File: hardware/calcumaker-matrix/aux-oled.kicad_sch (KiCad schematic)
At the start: 1 part, among them J3 OLED 128x32 (DNP)

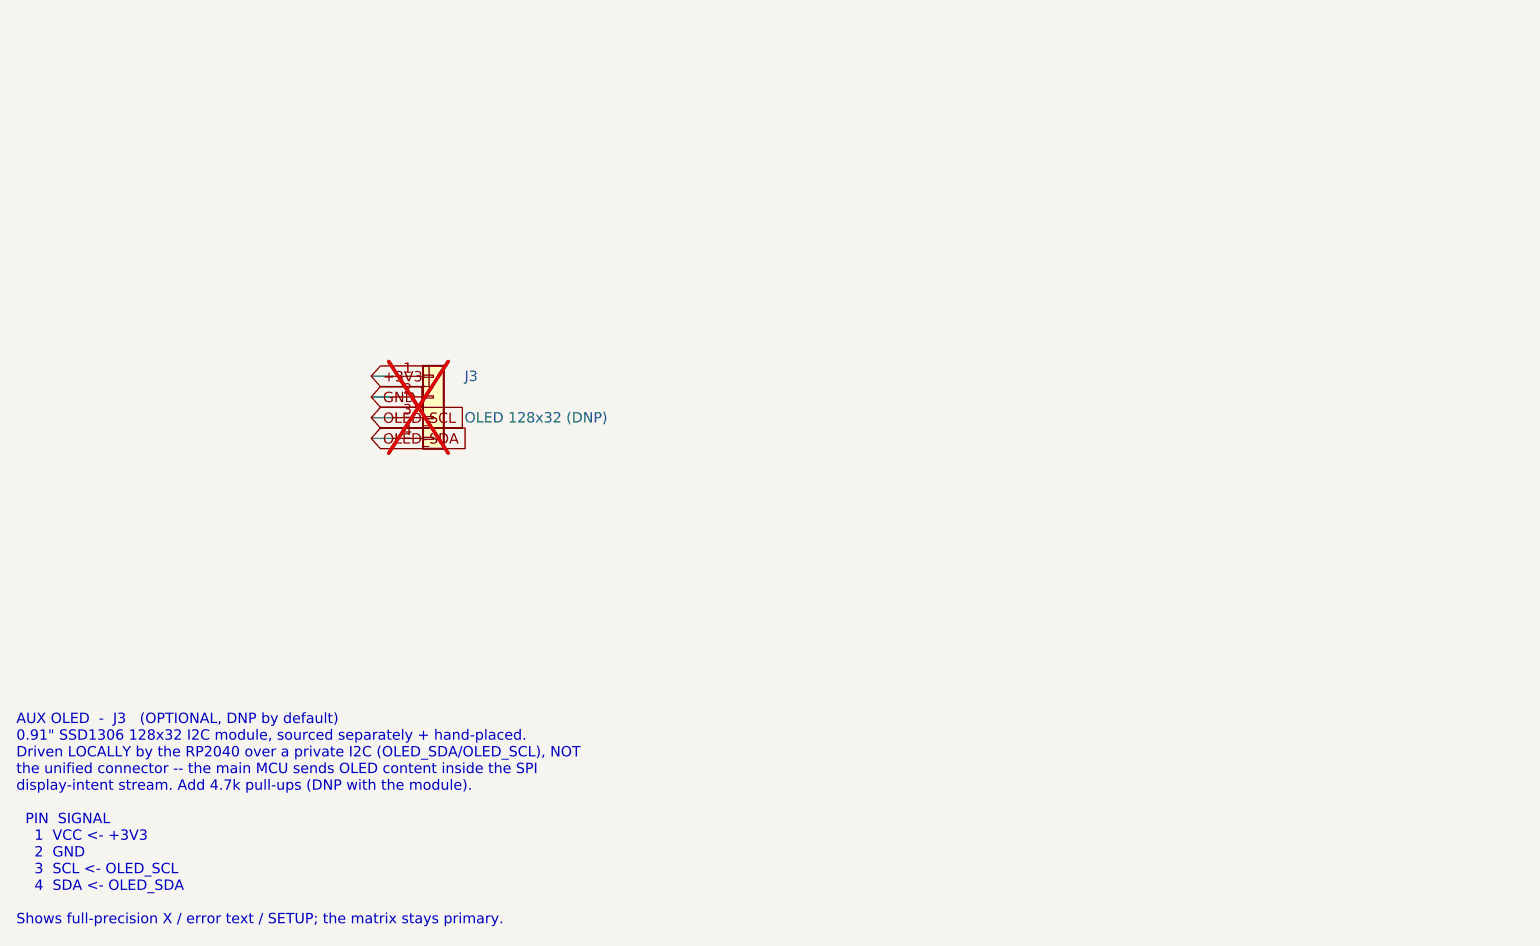
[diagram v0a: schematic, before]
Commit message: Floorplan both display PCBs and verify their schematic nets
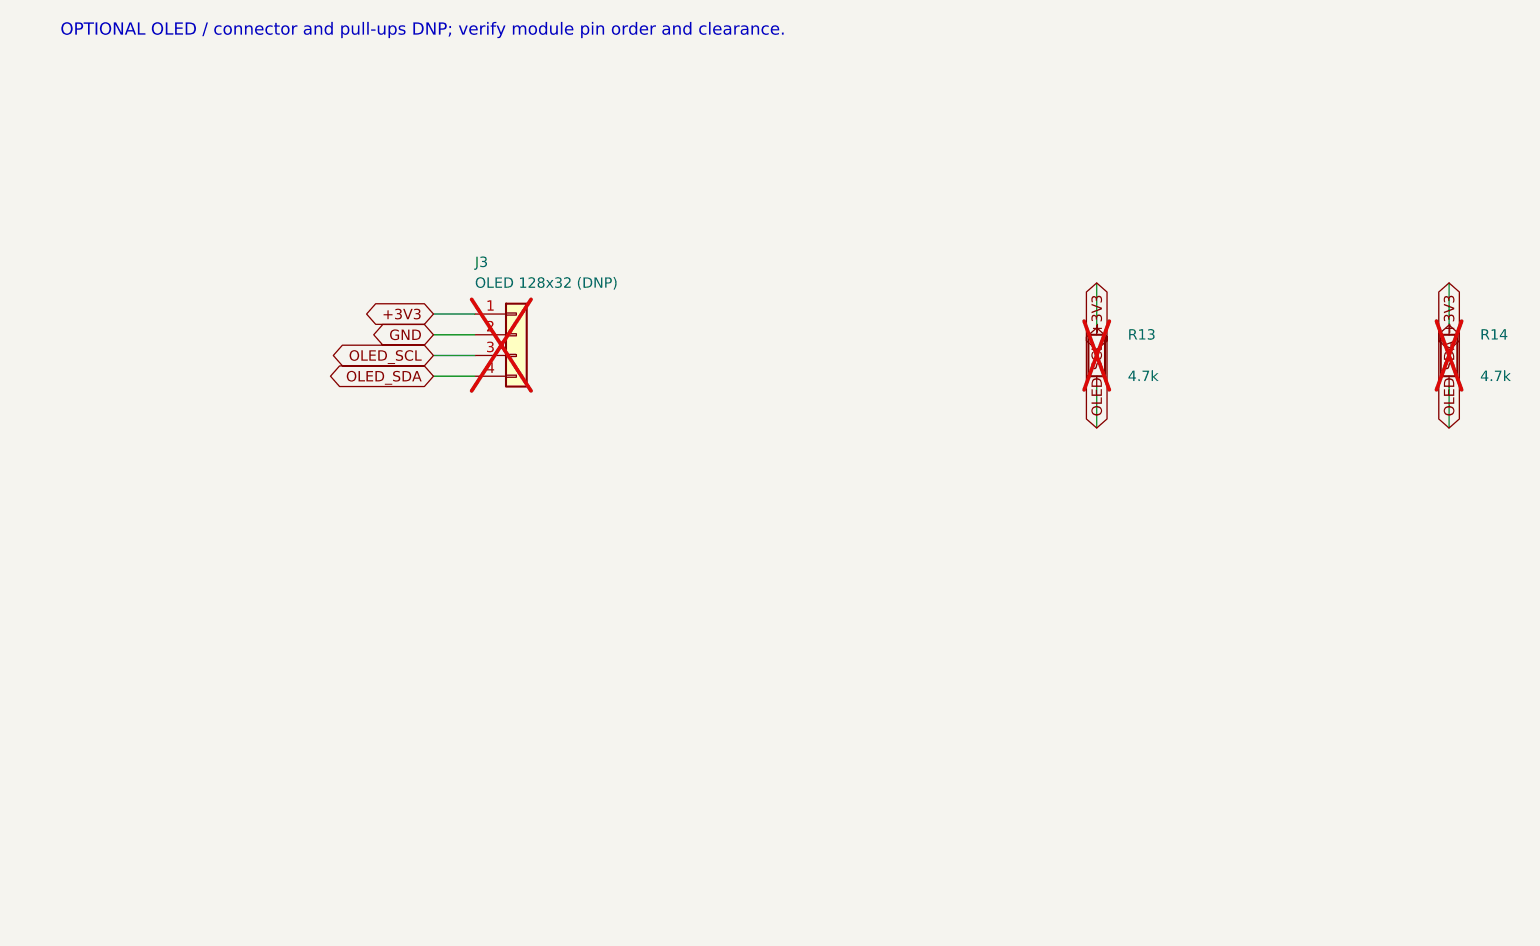
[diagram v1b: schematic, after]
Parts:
- added R13, R14: 4.7k, Resistor_SMD:R_0402_1005Metric, symbol Device:R
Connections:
- net +3V3: now also R13.1, R14.1
- net OLED_SCL: now also R13.2
- net OLED_SDA: now also R14.2
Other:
- note added: "OPTIONAL OLED / connector and pull-ups DNP; verify module pin order and clearance."
- note removed: "AUX OLED - J3 (OPTIONAL, DNP by default) 0.91" SSD1306 128x32 I2C module, sourced separately + hand-placed. Driven LOCALLY by the RP2040 over a private I2C (OLED_SDA/OLED_SCL), NOT the unified connector -- the main MCU sends OLED content inside the SPI display-intent stream. Add 4.7k pull-ups (DNP with the module). PIN SIGNAL 1 VCC <- +3V3 2 GND 3 SCL <- OLED_SCL 4 SDA <- OLED_SDA Shows full-prec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"
- title: Calcumaker 16 — RGB Matrix — Aux OLED 128x32 (SSD1306 I2C) — DNP-optional -> Calcumaker 16 / matrix / aux-oled
- moved on the sheet: J3
